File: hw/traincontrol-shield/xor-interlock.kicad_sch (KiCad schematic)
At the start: 4 parts, among them U3 74LVC1G86, U4 74LVC2G08

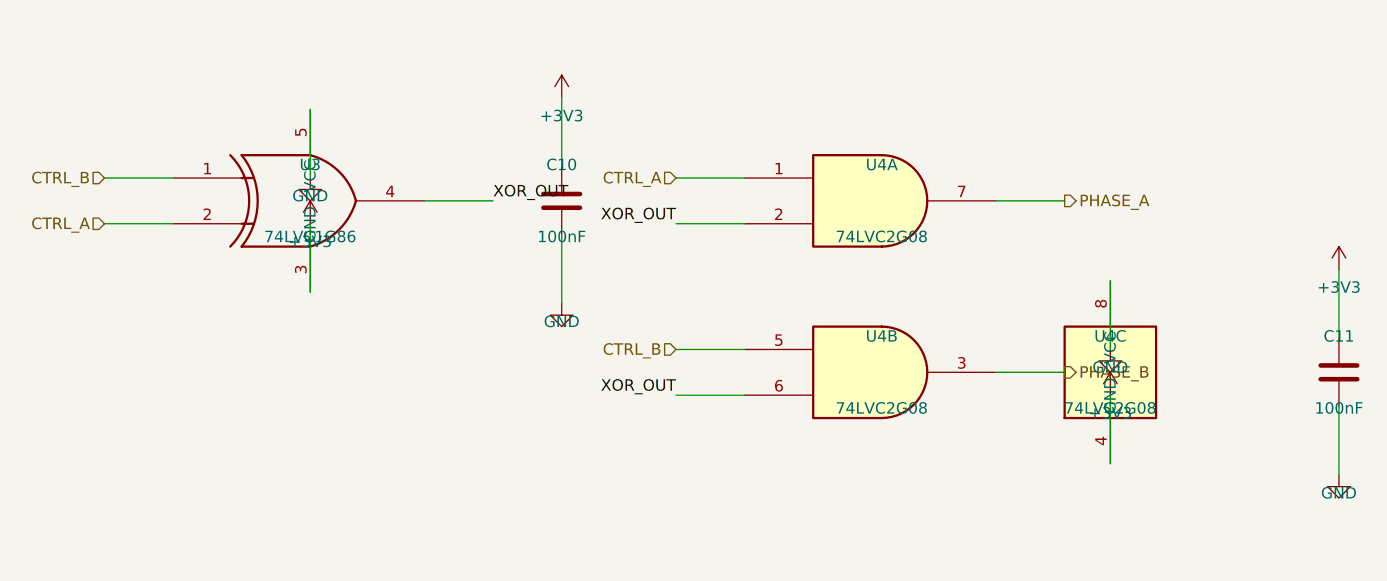
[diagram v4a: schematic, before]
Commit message: Fix power-symbol stub direction for vertical IC power pins
power_sym() assumed VCC pins are always at the top (stub UP) and GND at
the bottom (stub DOWN). SOT-23/VSSOP power units (74LVC1G86, 74LVC2G08)
have the opposite layout: VCC exits at the bottom, GND at the top.

Add angle=180 mode to power_sym() that flips the stub direction:
  angle=0   (default): VCC stub UP,   GND stub DOWN
  angle=180 (flipped):  VCC stub DOWN, GND stub UP

Apply angle=180 to U3 (74LVC1G86) and U4 (74LVC2G08) VCC/GND calls
in gen_xor_interlock so stubs exit away from the IC body.

Same docstring/logic fix applied to gen_power_supply.py's copy.

Co-Authored-By: Claude Sonnet 4.6 <noreply@anthropic.com>
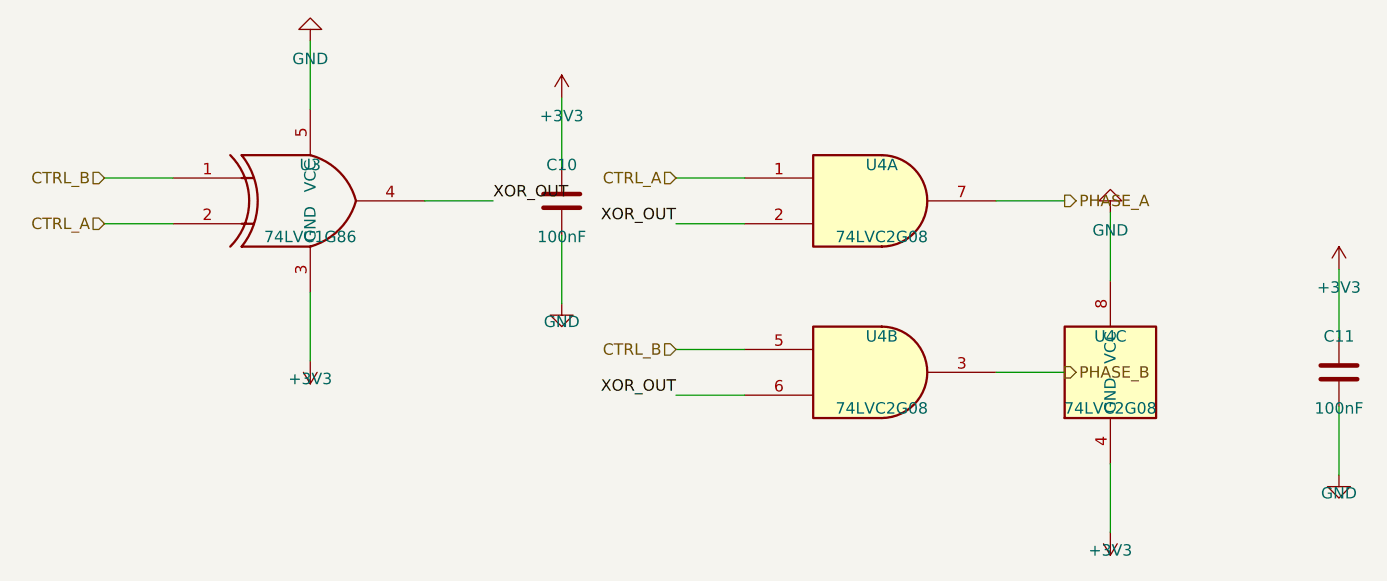
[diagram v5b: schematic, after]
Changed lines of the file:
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@@
 	)
 	(wire
-		(pts (xy 63.5 100.33) (xy 63.5 92.71))
+		(pts (xy 63.5 100.33) (xy 63.5 107.95))
 		(stroke (width 0) (type solid))
 	)
 	(symbol
 		(lib_id "power:+3V3")
-		(at 63.5 92.71 0)
+		(at 63.5 107.95 180)
 		(unit 1)
 		(exclude_from_sim no)
@@
 		(dnp no)
 		(property "Reference" "#PWR0401"
-			(at 63.5 90.71 0)
+			(at 63.5 105.95 0)
 			(effects (font (size 1.27 1.27)) (hide yes))
 		)
 		(property "Value" "+3V3"
-			(at 63.5 94.71 0)
-			(effects (font (size 1.27 1.27)))
-		)
-		(property "Footprint" ""
-			(at 63.5 92.71 0)
-			(effects (font (size 1.27 1.27)) (hide yes))
-		)
-		(property "Datasheet" ""
-			(at 63.5 92.71 0)
+			(at 63.5 109.95 0)
+			(effects (font (size 1.27 1.27)))
+		)
+		(property "Footprint" ""
+			(at 63.5 107.95 0)
+			(effects (font (size 1.27 1.27)) (hide yes))
+		)
+		(property "Datasheet" ""
+			(at 63.5 107.95 0)
 			(effects (font (size 1.27 1.27)) (hide yes))
 		)
@@
 	)
 	(wire
-		(pts (xy 63.5 80.01) (xy 63.5 87.63000000000001))
+		(pts (xy 63.5 80.01) (xy 63.5 72.39))
 		(stroke (width 0) (type solid))
 	)
 	(symbol
 		(lib_id "power:GND")
-		(at 63.5 87.63000000000001 0)
+		(at 63.5 72.39 180)
 		(unit 1)
 		(exclude_from_sim no)
@@
 		(dnp no)
 		(property "Reference" "#PWR0402"
-			(at 63.5 85.63000000000001 0)
+			(at 63.5 70.39 0)
 			(effects (font (size 1.27 1.27)) (hide yes))
 		)
 		(property "Value" "GND"
-			(at 63.5 89.63000000000001 0)
-			(effects (font (size 1.27 1.27)))
-		)
-		(property "Footprint" ""
-			(at 63.5 87.63000000000001 0)
-			(effects (font (size 1.27 1.27)) (hide yes))
-		)
-		(property "Datasheet" ""
-			(at 63.5 87.63000000000001 0)
+			(at 63.5 74.39 0)
+			(effects (font (size 1.27 1.27)))
+		)
+		(property "Footprint" ""
+			(at 63.5 72.39 0)
+			(effects (font (size 1.27 1.27)) (hide yes))
+		)
+		(property "Datasheet" ""
+			(at 63.5 72.39 0)
 			(effects (font (size 1.27 1.27)) (hide yes))
 		)
@@
 	)
 	(wire
-		(pts (xy 152.4 119.38) (xy 152.4 111.75999999999999))
+		(pts (xy 152.4 119.38) (xy 152.4 127.0))
 		(stroke (width 0) (type solid))
 	)
 	(symbol
 		(lib_id "power:+3V3")
-		(at 152.4 111.75999999999999 0)
+		(at 152.4 127.0 180)
 		(unit 1)
 		(exclude_from_sim no)
@@
 		(dnp no)
 		(property "Reference" "#PWR0405"
-			(at 152.4 109.75999999999999 0)
+			(at 152.4 125.0 0)
 			(effects (font (size 1.27 1.27)) (hide yes))
 		)
 		(property "Value" "+3V3"
-			(at 152.4 113.75999999999999 0)
-			(effects (font (size 1.27 1.27)))
-		)
-		(property "Footprint" ""
-			(at 152.4 111.75999999999999 0)
-			(effects (font (size 1.27 1.27)) (hide yes))
-		)
-		(property "Datasheet" ""
-			(at 152.4 111.75999999999999 0)
+			(at 152.4 129.0 0)
+			(effects (font (size 1.27 1.27)))
+		)
+		(property "Footprint" ""
+			(at 152.4 127.0 0)
+			(effects (font (size 1.27 1.27)) (hide yes))
+		)
+		(property "Datasheet" ""
+			(at 152.4 127.0 0)
 			(effects (font (size 1.27 1.27)) (hide yes))
 		)
@@
 	)
 	(wire
-		(pts (xy 152.4 99.06) (xy 152.4 106.68))
+		(pts (xy 152.4 99.06) (xy 152.4 91.44))
 		(stroke (width 0) (type solid))
 	)
 	(symbol
 		(lib_id "power:GND")
-		(at 152.4 106.68 0)
+		(at 152.4 91.44 180)
 		(unit 1)
 		(exclude_from_sim no)
@@
 		(dnp no)
 		(property "Reference" "#PWR0406"
-			(at 152.4 104.68 0)
+			(at 152.4 89.44 0)
 			(effects (font (size 1.27 1.27)) (hide yes))
 		)
 		(property "Value" "GND"
-			(at 152.4 108.68 0)
-			(effects (font (size 1.27 1.27)))
-		)
-		(property "Footprint" ""
-			(at 152.4 106.68 0)
-			(effects (font (size 1.27 1.27)) (hide yes))
-		)
-		(property "Datasheet" ""
-			(at 152.4 106.68 0)
-			(effects (font (size 1.27 1.27)) (hide yes))
-		)
+			(at 152.4 93.44 0)
+			(effects (font (size 1.27 1.27)))
+		)
+		(property "Footprint" ""
+			(at 152.4 91.44 0)
+			(effects (font (size 1.27 1.27)) (hide yes))
+		)
+		(property "Datasheet" ""
+			(at 152.4 91.44 0)
+			(effects (font (size 1.27 1.27)) (hide yes))
+		)

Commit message: Fix VCC/GND pin coordinates for U3/U4 power units; revert stub direction
The U3 (74LVC1G86) and U4 (74LVC2G08) pin y-coordinates were swapped:
VCC was listed at the bottom and GND at the top, opposite of the actual
KiCad symbol layout. This caused stubs to run into the IC body and
placed the wrong power net on each pin.

Corrected assignments (center y ∓ 10.16mm):
  U3: VCC pin5 at y=80.01 [top], GND pin3 at y=100.33 [bottom]
  U4: VCC pin8 at y=99.06  [top], GND pin4 at y=119.38 [bottom]

Reverts power_sym() to the original simple stub logic — VCC stub UP
(y-STUB), GND stub DOWN (y+STUB) — which is correct once the pin
positions are right.

Co-Authored-By: Claude Sonnet 4.6 <noreply@anthropic.com>
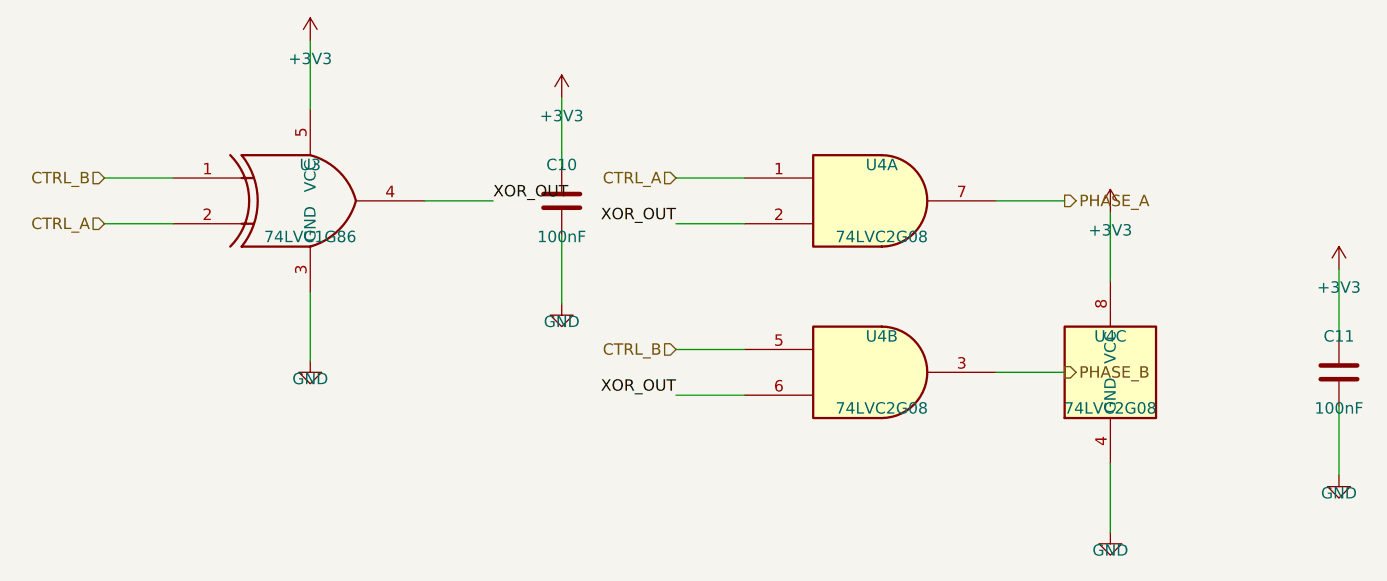
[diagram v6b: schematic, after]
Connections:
- net +3V3: now also U3.5 (VCC), U4.8 (VCC); no longer U3.3 (GND), U4.4 (GND)
- net GND: now also U3.3 (GND), U4.4 (GND); no longer U3.5 (VCC), U4.8 (VCC)
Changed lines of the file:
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@@
+	)
+	(wire
+		(pts (xy 63.5 80.01) (xy 63.5 72.39))
+		(stroke (width 0) (type solid))
+	)
+	(symbol
+		(lib_id "power:+3V3")
+		(at 63.5 72.39 0)
+		(unit 1)
+		(exclude_from_sim no)
+		(in_bom no)
+		(on_board yes)
+		(dnp no)
+		(property "Reference" "#PWR0401"
+			(at 63.5 70.39 0)
+			(effects (font (size 1.27 1.27)) (hide yes))
+		)
+		(property "Value" "+3V3"
+			(at 63.5 74.39 0)
+			(effects (font (size 1.27 1.27)))
+		)
+		(property "Footprint" ""
+			(at 63.5 72.39 0)
+			(effects (font (size 1.27 1.27)) (hide yes))
+		)
+		(property "Datasheet" ""
+			(at 63.5 72.39 0)
+			(effects (font (size 1.27 1.27)) (hide yes))
+		)
+		(pin "1")
+		(instances
+			(project "traincontrol-shield"
+				(path "/12cc2a67-9b1c-41e4-828f-9c2a8df6bb35/e0f8704d-1e30-470b-9f75-e6a1f31638d7"
+					(reference "#PWR0401")
+					(unit 1)
+				)
+			)
+		)
 	)
 	(wire
@@
 	)
 	(symbol
-		(lib_id "power:+3V3")
-		(at 63.5 107.95 180)
-		(unit 1)
-		(exclude_from_sim no)
-		(in_bom no)
-		(on_board yes)
-		(dnp no)
-		(property "Reference" "#PWR0401"
+		(lib_id "power:GND")
+		(at 63.5 107.95 0)
+		(unit 1)
+		(exclude_from_sim no)
+		(in_bom no)
+		(on_board yes)
+		(dnp no)
+		(property "Reference" "#PWR0402"
 			(at 63.5 105.95 0)
 			(effects (font (size 1.27 1.27)) (hide yes))
 		)
-		(property "Value" "+3V3"
+		(property "Value" "GND"
 			(at 63.5 109.95 0)
 			(effects (font (size 1.27 1.27)))
@@
 		(property "Datasheet" ""
 			(at 63.5 107.95 0)
-			(effects (font (size 1.27 1.27)) (hide yes))
-		)
-		(pin "1")
-		(instances
-			(project "traincontrol-shield"
-				(path "/12cc2a67-9b1c-41e4-828f-9c2a8df6bb35/e0f8704d-1e30-470b-9f75-e6a1f31638d7"
-					(reference "#PWR0401")
-					(unit 1)
-				)
-			)
-		)
-	)
-	(wire
-		(pts (xy 63.5 80.01) (xy 63.5 72.39))
-		(stroke (width 0) (type solid))
-	)
-	(symbol
-		(lib_id "power:GND")
-		(at 63.5 72.39 180)
-		(unit 1)
-		(exclude_from_sim no)
-		(in_bom no)
-		(on_board yes)
-		(dnp no)
-		(property "Reference" "#PWR0402"
-			(at 63.5 70.39 0)
-			(effects (font (size 1.27 1.27)) (hide yes))
-		)
-		(property "Value" "GND"
-			(at 63.5 74.39 0)
-			(effects (font (size 1.27 1.27)))
-		)
-		(property "Footprint" ""
-			(at 63.5 72.39 0)
-			(effects (font (size 1.27 1.27)) (hide yes))
-		)
-		(property "Datasheet" ""
-			(at 63.5 72.39 0)
 			(effects (font (size 1.27 1.27)) (hide yes))
 		)
@@
 	)
 	(wire
+		(pts (xy 152.4 99.06) (xy 152.4 91.44))
+		(stroke (width 0) (type solid))
+	)
+	(symbol
+		(lib_id "power:+3V3")
+		(at 152.4 91.44 0)
+		(unit 1)
+		(exclude_from_sim no)
+		(in_bom no)
+		(on_board yes)
+		(dnp no)
+		(property "Reference" "#PWR0405"
+			(at 152.4 89.44 0)
+			(effects (font (size 1.27 1.27)) (hide yes))
+		)
+		(property "Value" "+3V3"
+			(at 152.4 93.44 0)
+			(effects (font (size 1.27 1.27)))
+		)
+		(property "Footprint" ""
+			(at 152.4 91.44 0)
+			(effects (font (size 1.27 1.27)) (hide yes))
+		)
+		(property "Datasheet" ""
+			(at 152.4 91.44 0)
+			(effects (font (size 1.27 1.27)) (hide yes))
+		)
+		(pin "1")
+		(instances
+			(project "traincontrol-shield"
+				(path "/12cc2a67-9b1c-41e4-828f-9c2a8df6bb35/e0f8704d-1e30-470b-9f75-e6a1f31638d7"
+					(reference "#PWR0405")
+					(unit 1)
+				)
+			)
+		)
+	)
+	(wire
 		(pts (xy 152.4 119.38) (xy 152.4 127.0))
 		(stroke (width 0) (type solid))
 	)
 	(symbol
-		(lib_id "power:+3V3")
-		(at 152.4 127.0 180)
-		(unit 1)
-		(exclude_from_sim no)
-		(in_bom no)
-		(on_board yes)
-		(dnp no)
-		(property "Reference" "#PWR0405"
+		(lib_id "power:GND")
+		(at 152.4 127.0 0)
+		(unit 1)
+		(exclude_from_sim no)
+		(in_bom no)
+		(on_board yes)
+		(dnp no)
+		(property "Reference" "#PWR0406"
 			(at 152.4 125.0 0)
 			(effects (font (size 1.27 1.27)) (hide yes))
 		)
-		(property "Value" "+3V3"
+		(property "Value" "GND"
 			(at 152.4 129.0 0)
 			(effects (font (size 1.27 1.27)))
@@
 			(effects (font (size 1.27 1.27)) (hide yes))
 		)
-		(pin "1")
-		(instances
-			(project "traincontrol-shield"
-				(path "/12cc2a67-9b1c-41e4-828f-9c2a8df6bb35/e0f8704d-1e30-470b-9f75-e6a1f31638d7"
-					(reference "#PWR0405")
-					(unit 1)
-				)
-			)
-		)
-	)
-	(wire
-		(pts (xy 152.4 99.06) (xy 152.4 91.44))
-		(stroke (width 0) (type solid))
-	)
-	(symbol
-		(lib_id "power:GND")
-		(at 152.4 91.44 180)
-		(unit 1)
-		(exclude_from_sim no)
-		(in_bom no)
-		(on_board yes)
-		(dnp no)
-		(property "Reference" "#PWR0406"
-			(at 152.4 89.44 0)
-			(effects (font (size 1.27 1.27)) (hide yes))
-		)
-		(property "Value" "GND"
-			(at 152.4 93.44 0)
-			(effects (font (size 1.27 1.27)))
-		)
-		(property "Footprint" ""
-			(at 152.4 91.44 0)
-			(effects (font (size 1.27 1.27)) (hide yes))
-		)
-		(property "Datasheet" ""
-			(at 152.4 91.44 0)
-			(effects (font (size 1.27 1.27)) (hide yes))
-		)
